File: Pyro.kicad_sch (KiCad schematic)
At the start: 35 parts, among them J12 Conn_01x02_Male, Q1 SSM3K15AMFV,L3F, Q2 BUK9M11-40EX, U6 SiC437BED-T1-GE3, U8 TPS259621DDAT, U9 859-LTV-247

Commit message: Review 1 Changes Complete
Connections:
- net +12V renamed DeployV
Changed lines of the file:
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@@
-    (effects (font (size 1.27 1.27)) (justify right bottom))
-  )
-  (label "+12V" (at 245.364 117.602 180) (fields_autoplaced)
     (effects (font (size 1.27 1.27)) (justify right bottom))
   )
@@
   (label "SW" (at 174.244 75.692 180) (fields_autoplaced)
     (effects (font (size 1.27 1.27)) (justify right bottom))
+  )
+  (global_label "DeployV" (shape bidirectional) (at 245.364 117.602 90) (fields_autoplaced)
+    (effects (font (size 1.27 1.27)) (justify left))
+    (property "Intersheetrefs" "${INTERSHEET_REFS}" (at 245.364 106.9405 90)
+      (effects (font (size 1.27 1.27)) (justify left) hide)
+    )
+  )
+  (global_label "DeployV" (shape bidirectional) (at 209.804 90.932 0) (fields_autoplaced)
+    (effects (font (size 1.27 1.27)) (justify left))
+    (property "Intersheetrefs" "${INTERSHEET_REFS}" (at 220.4655 90.932 0)
+      (effects (font (size 1.27 1.27)) (justify left) hide)
+    )
+  )
+  (global_label "DeployV" (shape bidirectional) (at 209.804 80.772 0) (fields_autoplaced)
+    (effects (font (size 1.27 1.27)) (justify left))
+    (property "Intersheetrefs" "${INTERSHEET_REFS}" (at 220.4655 80.772 0)
+      (effects (font (size 1.27 1.27)) (justify left) hide)
+    )
+  )
+  (global_label "DeployV" (shape bidirectional) (at 111.252 160.274 90) (fields_autoplaced)
+    (effects (font (size 1.27 1.27)) (justify left))
+    (property "Intersheetrefs" "${INTERSHEET_REFS}" (at 111.252 149.6125 90)
+      (effects (font (size 1.27 1.27)) (justify left) hide)
+    )
+  )
+  (global_label "DeployV" (shape bidirectional) (at 172.974 66.802 90) (fields_autoplaced)
+    (effects (font (size 1.27 1.27)) (justify left))
+    (property "Intersheetrefs" "${INTERSHEET_REFS}" (at 172.974 56.1405 90)
+      (effects (font (size 1.27 1.27)) (justify left) hide)
+    )
   )
   (hierarchical_label "Cont1" (shape output) (at 95.758 55.626 180) (fields_autoplaced)
@@
         (path "/7db990e4-92e1-4f99-b4d2-435bbec1ba83/3c6662b6-8783-49dc-b944-3dc2b3e30a07"
           (reference "#PWR0159") (unit 1)
-        )
-      )
-    )
-  )
-  (symbol (lib_id "power:+12V") (at 209.804 80.772 0) (unit 1)
-    (in_bom yes) (on_board yes) (dnp no) (fields_autoplaced)
-    (property "Reference" "#PWR068" (at 209.804 84.582 0)
-      (effects (font (size 1.27 1.27)) hide)
-    )
-    (property "Value" "+12V" (at 209.804 77.1962 0)
-      (effects (font (size 1.27 1.27)))
-    )
-    (property "Footprint" "" (at 209.804 80.772 0)
-      (effects (font (size 1.27 1.27)) hide)
-    )
-    (property "Datasheet" "" (at 209.804 80.772 0)
-      (effects (font (size 1.27 1.27)) hide)
-    )
-    (pin "1")
-    (instances
-      (project "Ricardo-Stark"
-        (path "/7db990e4-92e1-4f99-b4d2-435bbec1ba83/6c17bf58-bab3-4fa6-ad33-cca9e388d73c"
-          (reference "#PWR068") (unit 1)
-        )
-        (path "/7db990e4-92e1-4f99-b4d2-435bbec1ba83/3c6662b6-8783-49dc-b944-3dc2b3e30a07"
-          (reference "#PWR0157") (unit 1)
         )
       )
@@
     )
   )
-  (symbol (lib_id "power:+12V") (at 172.974 66.802 0) (unit 1)
-    (in_bom yes) (on_board yes) (dnp no) (fields_autoplaced)
-    (property "Reference" "#PWR068" (at 172.974 70.612 0)
-      (effects (font (size 1.27 1.27)) hide)
-    )
-    (property "Value" "+12V" (at 172.974 63.2262 0)
-      (effects (font (size 1.27 1.27)))
-    )
-    (property "Footprint" "" (at 172.974 66.802 0)
-      (effects (font (size 1.27 1.27)) hide)
-    )
-    (property "Datasheet" "" (at 172.974 66.802 0)
-      (effects (font (size 1.27 1.27)) hide)
-    )
-    (pin "1")
-    (instances
-      (project "Ricardo-Stark"
-        (path "/7db990e4-92e1-4f99-b4d2-435bbec1ba83/6c17bf58-bab3-4fa6-ad33-cca9e388d73c"
-          (reference "#PWR068") (unit 1)
-        )
-        (path "/7db990e4-92e1-4f99-b4d2-435bbec1ba83/3c6662b6-8783-49dc-b944-3dc2b3e30a07"
-          (reference "#PWR0154") (unit 1)
-        )
-      )
-    )
-  )
   (symbol (lib_id "Device:C_Small") (at 32.258 114.808 90) (unit 1)
     (in_bom yes) (on_board yes) (dnp no) (fields_autoplaced)
@@
     )
   )
-  (symbol (lib_id "power:+12V") (at 111.252 160.274 0) (unit 1)
-    (in_bom yes) (on_board yes) (dnp no) (fields_autoplaced)
-    (property "Reference" "#PWR063" (at 111.252 164.084 0)
-      (effects (font (size 1.27 1.27)) hide)
-    )
-    (property "Value" "+12V" (at 111.252 156.6982 0)
-      (effects (font (size 1.27 1.27)))
-    )
-    (property "Footprint" "" (at 111.252 160.274 0)
-      (effects (font (size 1.27 1.27)) hide)
-    )
-    (property "Datasheet" "" (at 111.252 160.274 0)
-      (effects (font (size 1.27 1.27)) hide)
-    )
-    (pin "1")
-    (instances
-      (project "Ricardo-Stark"
-        (path "/7db990e4-92e1-4f99-b4d2-435bbec1ba83/6c17bf58-bab3-4fa6-ad33-cca9e388d73c"
-          (reference "#PWR063") (unit 1)
-        )
-        (path "/7db990e4-92e1-4f99-b4d2-435bbec1ba83/3c6662b6-8783-49dc-b944-3dc2b3e30a07"
-          (reference "#PWR0175") (unit 1)
-        )
-      )
-    )
-  )
   (symbol (lib_id "Device:R") (at 103.378 59.436 0) (unit 1)
     (in_bom yes) (on_board yes) (dnp no) (fields_autoplaced)
@@
         )
       )
-    )
-  )
-  (symbol (lib_id "power:+12V") (at 209.804 90.932 0) (unit 1)
-    (in_bom yes) (on_board yes) (dnp no) (fields_autoplaced)
-    (property "Reference" "#PWR068" (at 209.804 94.742 0)
-      (effects (font (size 1.27 1.27)) hide)
-    )
-    (property "Value" "+12V" (at 209.804 87.3562 0)
-      (effects (font (size 1.27 1.27)))
-    )
-    (property "Footprint" "" (at 209.804 90.932 0)
-      (effects (font (size 1.27 1.27)) hide)
-    )
-    (property "Datasheet" "" (at 209.804 90.932 0)
-      (effects (font (size 1.27 1.27)) hide)
-    )
-    (pin "1")
-    (instances
-      (project "Ricardo-Stark"
-        (path "/7db990e4-92e1-4f99-b4d2-435bbec1ba83/6c17bf58-bab3-4fa6-ad33-cca9e388d73c"
-          (reference "#PWR068") (unit 1)
-        )
-        (path "/7db990e4-92e1-4f99-b4d2-435bbec1ba83/3c6662b6-8783-49dc-b944-3dc2b3e30a07"
-          (reference "#PWR0158") (unit 1)
-        )
-      )

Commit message: Take 3
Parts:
- removed Q1: SSM3K15AMFV,L3F, Package_TO_SOT_SMD:SOT-723, symbol Device:Q_NMOS_GSD
- removed R24: 1k, Resistor_SMD:R_0402_1005Metric, symbol Device:R_Small
- added C33 (x2): 47uF, Capacitor_SMD:C_1206_3216Metric, symbol Device:C_Small
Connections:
- net DeployV: now also C33.1
- net EFuse_In: now also C33.1
- net GND: now also C33.2, C33.2
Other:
- moved on the sheet: C28, C34, R75

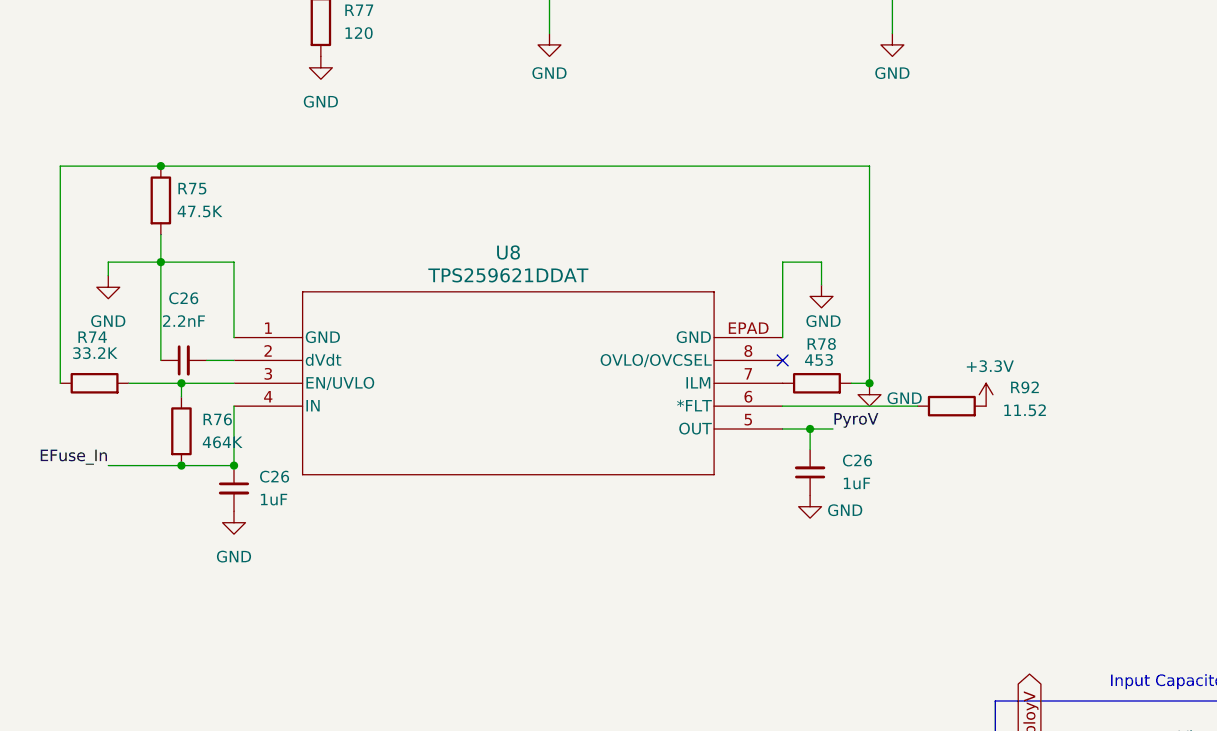
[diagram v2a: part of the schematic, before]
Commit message: Sized sensor resistors and more routing
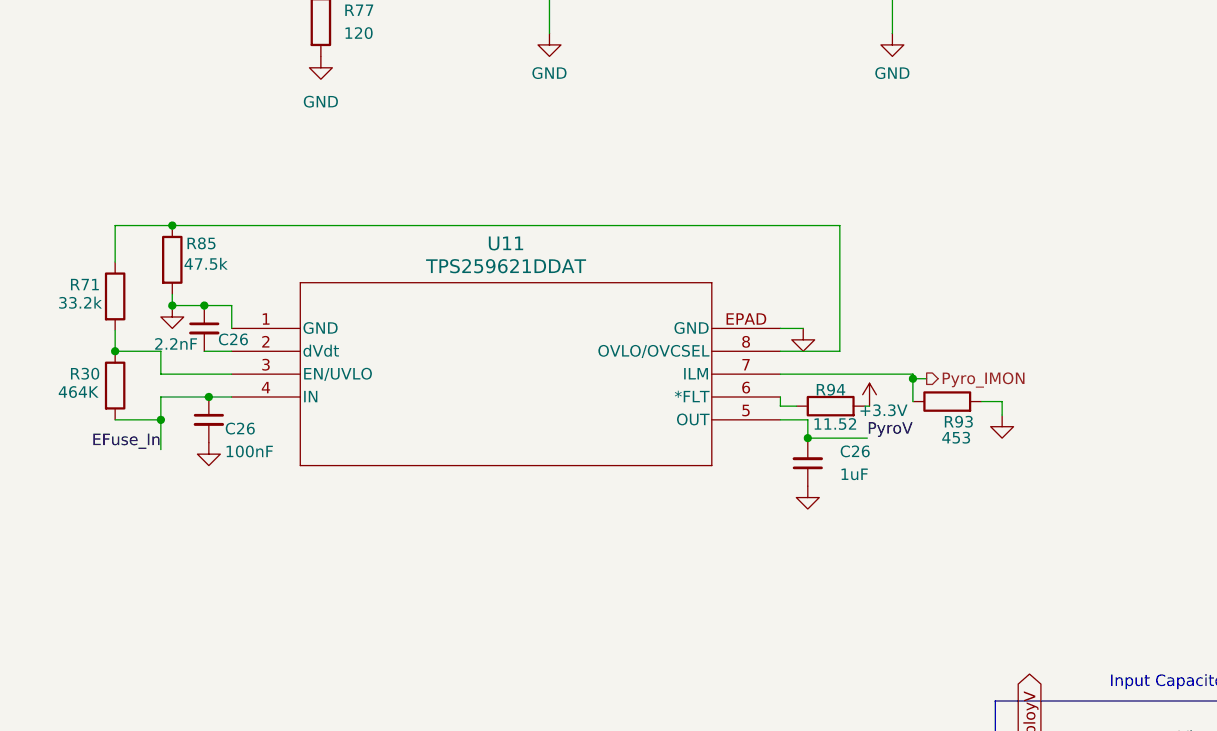
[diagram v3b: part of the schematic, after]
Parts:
- removed C26: 1uF, Capacitor_SMD:C_0402_1005Metric, symbol Device:C_Small
- removed C26: 2.2nF, Capacitor_SMD:C_0402_1005Metric, symbol Device:C_Small
- removed C26: 1uF, Capacitor_SMD:C_0603_1608Metric, symbol Device:C_Small
- removed R74: 33.2K, Resistor_SMD:R_0402_1005Metric, symbol Device:R
- removed R75: 47.5K, Resistor_SMD:R_0402_1005Metric, symbol Device:R
- removed R76: 464K, Resistor_SMD:R_0402_1005Metric, symbol Device:R
- removed R78: 453, Resistor_SMD:R_0402_1005Metric, symbol Device:R
- removed R92: 11.52, Resistor_SMD:R_0402_1005Metric, symbol Device:R
- removed U8: TPS259621DDAT, EFuse:SO-PP-DDA-8_TEX, symbol EFuse:TPS259621DDAT
- added C26: 2.2nF, Capacitor_SMD:C_0402_1005Metric, symbol Device:C_Small
- added C26: 100nF, Capacitor_SMD:C_0402_1005Metric, symbol Device:C_Small
- added C26: 1uF, Capacitor_SMD:C_0603_1608Metric, symbol Device:C_Small
- added R30: 464K, Resistor_SMD:R_0402_1005Metric, symbol Device:R
- added R71: 33.2k, Resistor_SMD:R_0402_1005Metric, symbol Device:R
- added R85: 47.5k, Resistor_SMD:R_0402_1005Metric, symbol Device:R
- added R93: 453, Resistor_SMD:R_0402_1005Metric, symbol Device:R
- added R94: 11.52, Resistor_SMD:R_0402_1005Metric, symbol Device:R
- added U11: TPS259621DDAT, EFuse:SO-PP-DDA-8_TEX, symbol EFuse:TPS259621DDAT
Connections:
- net +3V3: now also R94.2
- net EFuse_In: now also C26.1, R30.2, U11.4 (IN)
- net GND: now also C26.1, C26.1, C26.2, R85.2, R93.2, U11.1 (GND), U11.EPAD (GND)
- net PyroV: now also C26.2, U11.5 (OUT)
- new net: R30.1, R71.2, U11.3 (EN/UVLO)
- new net: C26.2, U11.2 (dVdt)
- new net: R94.1, U11.6 (*FLT)
- new net: R71.1, R85.1, U11.8 (OVLO/OVCSEL)
- new net Pyro_IMON: R93.1, U11.7 (ILM)
- no-connect marks 4 -> 3

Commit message: review changes
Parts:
- renumbered C33 to C40, C25 to C73, C26 to C74, C33 to C75, C35 to C76, C28 to C80, C34 to C83, C33 to C85, C26 to C86, C26 to C87, C26 to C88, L4 to L7, R19 to R81, R20 to R82, R21 to R83, R22 to R84, R25 to R86, R26 to R87, R27 to R88, U6 to U10

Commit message: review changes
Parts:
- added R42: 30k, Resistor_SMD:R_0402_1005Metric, symbol Device:R
- added R43: 10k, Resistor_SMD:R_0402_1005Metric, symbol Device:R
- R94: value 11.52 -> 470
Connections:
- net GND: now also R43.1
- net PyroV: now also R42.1
- new net Fuse_Cont: R42.2, R43.2

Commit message: artem big brain moment
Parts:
- removed C87: 2.2nF, Capacitor_SMD:C_0402_1005Metric, symbol Device:C_Small
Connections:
- no-connect marks 3 -> 4
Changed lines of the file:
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@@
-	)
-	(junction
-		(at 34.544 108.712)
-		(diameter 0)
-		(color 0 0 0 0)
 	)
 	(junction
@@
 	)
 	(no_connect
+		(at 37.592 113.792)
+	)
+	(no_connect
 		(at 209.804 96.012)
 	)
@@
 		)
 	)
-	(wire
-		(pts
-			(xy 34.544 113.792) (xy 37.592 113.792)
-		)
-		(stroke
-			(width 0)
-			(type default)
-		)
-	)
 	(polyline
 		(pts
@@
 	(wire
 		(pts
-			(xy 30.988 108.712) (xy 34.544 108.712)
+			(xy 30.988 108.712) (xy 37.592 108.712)
 		)
 		(stroke
@@
 		(pts
 			(xy 118.618 55.626) (xy 118.618 64.516)
-		)
-		(stroke
-			(width 0)
-			(type default)
-		)
-	)
-	(wire
-		(pts
-			(xy 37.592 108.712) (xy 34.544 108.712)
 		)
 		(stroke
@@
 					(unit 1)
 				)
-			)
-		)
-	)
-	(symbol
-		(lib_id "Device:C_Small")
-		(at 34.544 111.252 0)
-		(unit 1)
-		(exclude_from_sim no)
-		(in_bom yes)
-		(on_board yes)
-		(dnp no)
-		(property "Reference" "C87"
-			(at 36.068 112.522 0)
-			(effects
-				(font
-					(size 1.27 1.27)
-				)
-				(justify left)
-			)
-		)
-		(property "Value" "2.2nF"
-			(at 28.956 113.03 0)
-			(effects
-				(font
-					(size 1.27 1.27)
-				)
-				(justify left)
-			)
-		)
-		(property "Footprint" "Capacitor_SMD:C_0402_1005Metric"
-			(at 34.544 111.252 0)
-			(effects
-				(font
-					(size 1.27 1.27)
-				)
-				(hide yes)
-			)
-		)
-		(property "Datasheet" "~"
-			(at 34.544 111.252 0)
-			(effects
-				(font
-					(size 1.27 1.27)
-				)
-				(hide yes)
-			)
-		)
-		(property "Description" ""
-			(at 34.544 111.252 0)
-			(effects
-				(font
-					(size 1.27 1.27)
-				)
-				(hide yes)
-			)
-		)
-		(pin "1"
-		)
-		(pin "2"
-		)
-		(instances
-			(project "Ricardo-Stark"
-				(path "/7db990e4-92e1-4f99-b4d2-435bbec1ba83/3c6662b6-8783-49dc-b944-3dc2b3e30a07"
-					(reference "C87")
-					(unit 1)
-				)

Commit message: more changes
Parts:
- removed C86: 100nF, Capacitor_SMD:C_0402_1005Metric, symbol Device:C_Small
- removed C88: 1uF, Capacitor_SMD:C_0603_1608Metric, symbol Device:C_Small
- removed R30: 464K, Resistor_SMD:R_0402_1005Metric, symbol Device:R
- removed R71: 33.2k, Resistor_SMD:R_0402_1005Metric, symbol Device:R
- removed R85: 47.5k, Resistor_SMD:R_0402_1005Metric, symbol Device:R
- removed R93: 453, Resistor_SMD:R_0402_1005Metric, symbol Device:R
- removed R94: 470, Resistor_SMD:R_0402_1005Metric, symbol Device:R
- removed U11: TPS259621DDAT, EFuse:SO-PP-DDA-8_TEX, symbol EFuse:TPS259621DDAT
- added C45: 4.7nF, Capacitor_SMD:C_0402_1005Metric, symbol Device:C_Small
- added C46: 10nF, Capacitor_SMD:C_0402_1005Metric, symbol Device:C_Small
- added IC5: TPS259830ONRGER, iclr:TPS259830ONRGER, symbol iclr:TPS259830ONRGER
- added R108: 1M, Capacitor_SMD:C_0402_1005Metric, symbol Device:R_Small
- added R109: 732k, Capacitor_SMD:C_0402_1005Metric, symbol Device:R_Small
- added R110: 73.2k, Capacitor_SMD:C_0402_1005Metric, symbol Device:R_Small
- added R111: 300, Capacitor_SMD:C_0402_1005Metric, symbol Device:R_Small
- added R112: 681, Capacitor_SMD:C_0402_1005Metric, symbol Device:R_Small
- added R113: 100k, Capacitor_SMD:C_0402_1005Metric, symbol Device:R_Small
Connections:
- net +3V3: now also R113.1
- net EFuse_In: now also C46.2, IC5.1 (IN_1), IC5.16 (IN_4), IC5.2 (IN_2), IC5.25 (IN_5), IC5.3 (IN_3), R108.1
- net GND: now also C45.1, C46.1, IC5.11 (NRETRY), IC5.14 (GND_3), IC5.26 (GND_4), IC5.4 (GND_1), IC5.5 (GND_2), R110.2, R111.2, R112.2
- net PyroV: now also IC5.17 (OUT_1), IC5.18 (OUT_2), IC5.19 (OUT_3), IC5.20 (OUT_4), IC5.21 (OUT_5), IC5.22 (OUT_6), IC5.23 (OUT_7), IC5.24 (OUT_8)
- net Pyro_IMON: now also IC5.9 (IMON), R112.1
- new net: IC5.8 (ILIM), R111.1
- new net: C45.2, IC5.7 (ITIMER)
- new net: IC5.13 (PG), R113.2
- new net: IC5.6 (EN/UVLO), R108.2, R109.1
- new net OVLO: IC5.12 (OVLO), R109.2, R110.1
- no-connect marks 4 -> 5
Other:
- note added: "dvdt pin left floating for fastest turn on time"
